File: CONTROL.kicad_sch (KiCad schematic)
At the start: 91 parts, among them J1 RJ45_Hanrun_HR911105A_Horizon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, J9 DISP, M1 Fan_4pin, M2 Fan_4pin, Q1 BSS138, Q2 BSS138, SW1 SW_Omron_B3F-315x, U1 TMP102xxDRL, U12 W5500, U13 TMP102xxDRL, X1 TXM25M0004322JBDDO00T

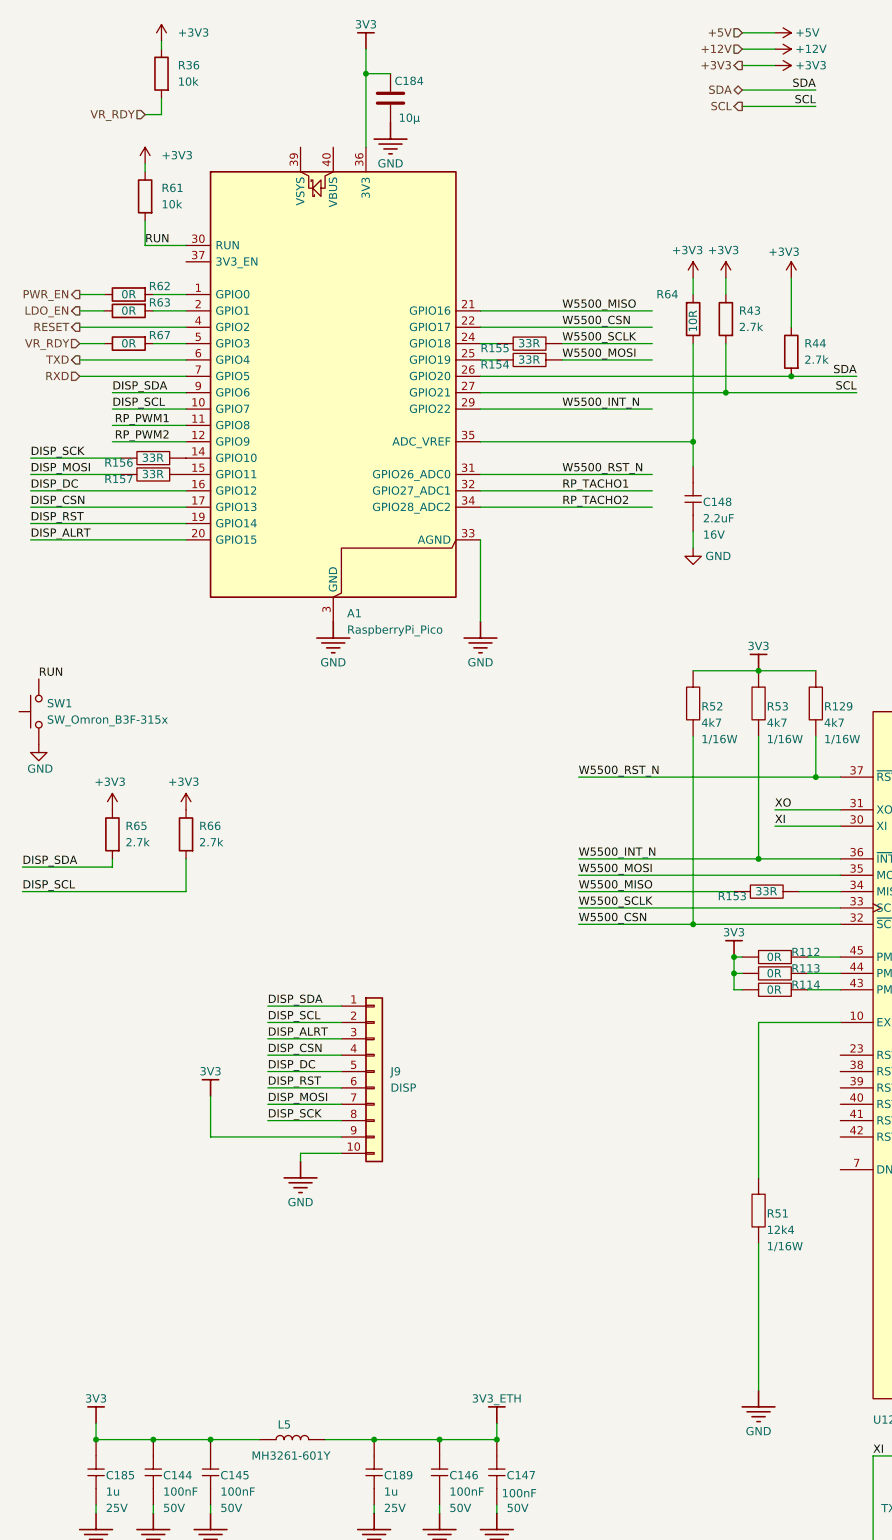
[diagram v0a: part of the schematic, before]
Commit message: W5500 ROUTED
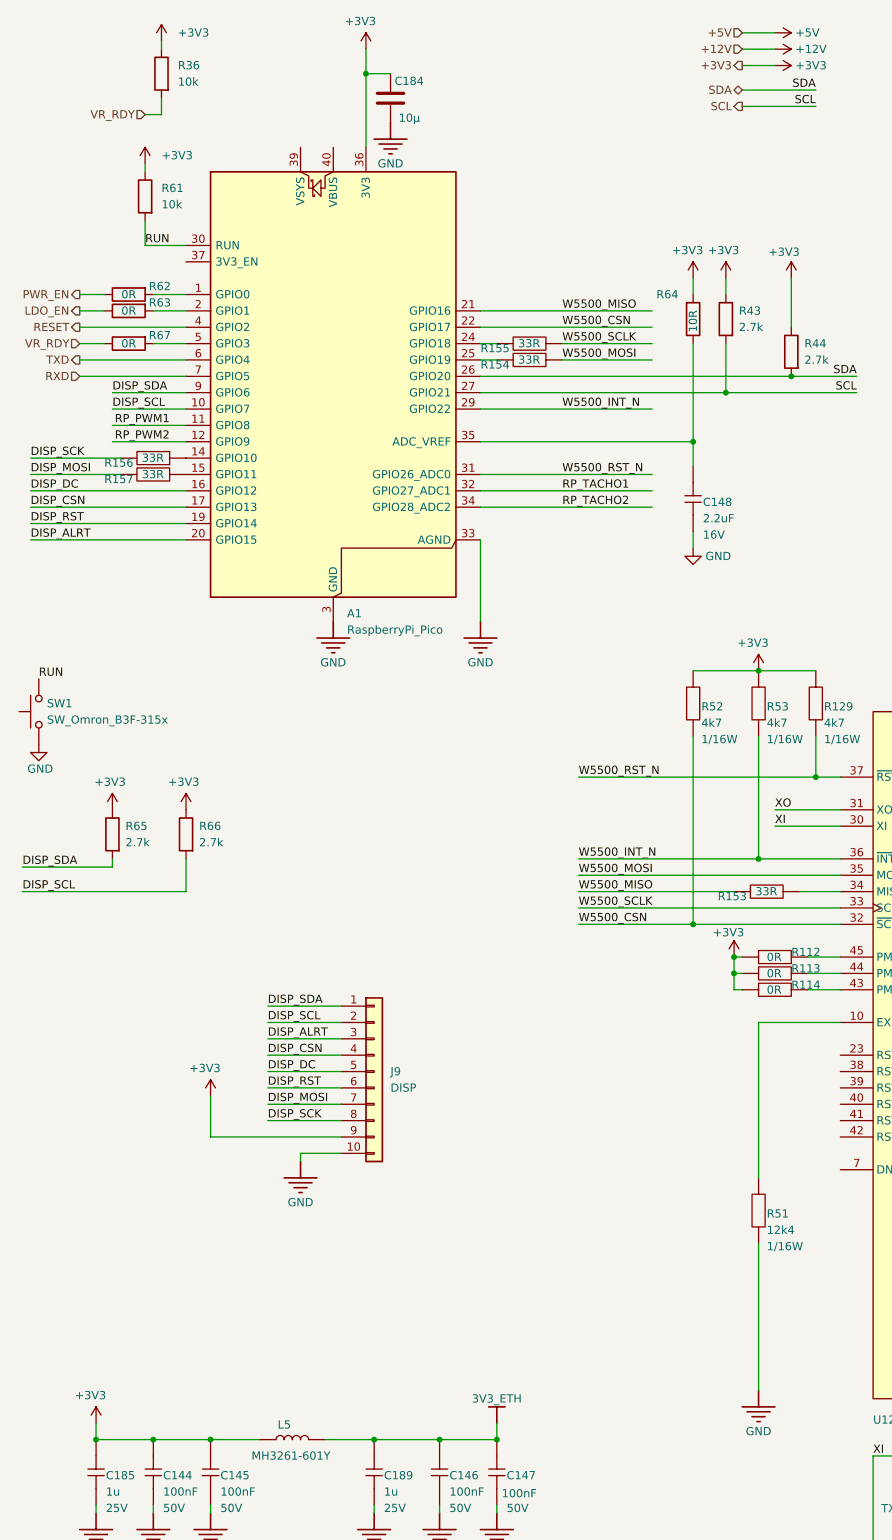
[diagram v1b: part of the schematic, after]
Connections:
- net 3V3 is gone; now on net +3V3: A1.36 (3V3), C144.1, C145.1, C184.1, C185.1, J9.9 (Pin_9), L5.1, R112.2, R113.2, R114.2, R129.2, R52.2, R53.2

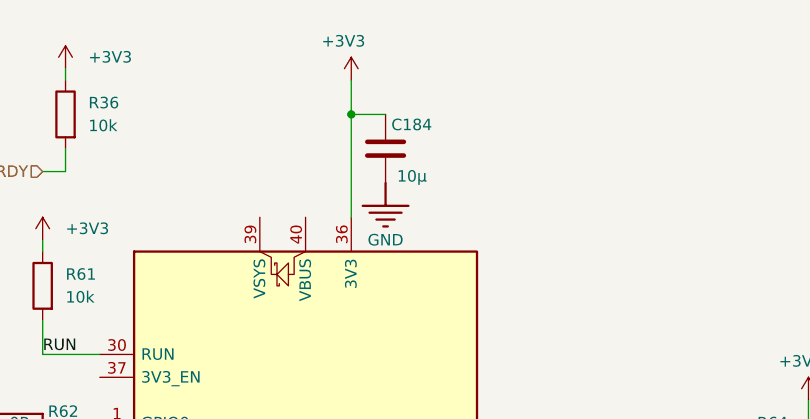
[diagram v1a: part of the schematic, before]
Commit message: logic dc bucks routed
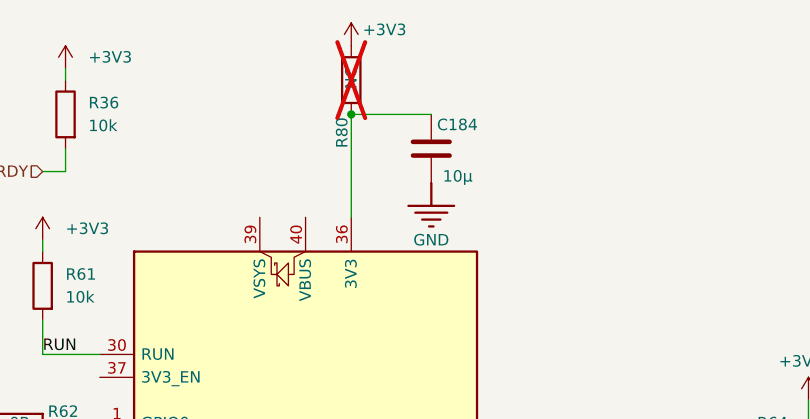
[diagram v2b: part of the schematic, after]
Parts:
- added R80: NC, Resistor_SMD:R_0603_1608Metric, symbol Device:R
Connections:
- net +3V3: now also R80.2; no longer A1.36 (3V3), C184.1
- new net: A1.36 (3V3), C184.1, R80.1
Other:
- moved on the sheet: C184
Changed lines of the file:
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@@
 	)
 	(junction
-		(at 72.39 25.4)
-		(diameter 0)
-		(color 0 0 0 0)
-	)
-	(junction
 		(at 234.95 167.64)
 		(diameter 0)
@@
 	)
 	(junction
+		(at 72.39 25.4)
+		(diameter 0)
+		(color 0 0 0 0)
+	)
+	(junction
 		(at 30.48 237.49)
 		(diameter 0)
@@
 	(wire
 		(pts
-			(xy 72.39 25.4) (xy 76.2 25.4)
+			(xy 72.39 25.4) (xy 81.28 25.4)
 		)
 		(stroke
@@
 	(wire
 		(pts
-			(xy 72.39 21.59) (xy 72.39 25.4)
-		)
-		(stroke
-			(width 0)
-			(type default)
-		)
-	)
-	(wire
-		(pts
 			(xy 83.82 248.92) (xy 83.82 247.65)
 		)
@@
 	(symbol
 		(lib_id "IMPORT-altium-import:GND_POWER_GROUND")
-		(at 76.2 33.02 0)
+		(at 81.28 33.02 0)
 		(unit 1)
 		(body_style 1)
@@
 		(dnp no)
 		(property "Reference" "#PWR0264"
-			(at 76.2 33.02 0)
+			(at 81.28 33.02 0)
 			(hide yes)
 			(show_name no)
@@
 		)
 		(property "Value" "GND"
-			(at 76.2 39.37 0)
+			(at 81.28 39.37 0)
 			(show_name no)
 			(do_not_autoplace no)
@@
 		)
 		(property "Footprint" ""
-			(at 76.2 33.02 0)
+			(at 81.28 33.02 0)
 			(show_name no)
 			(do_not_autoplace no)
@@
 		)
 		(property "Datasheet" ""
-			(at 76.2 33.02 0)
+			(at 81.28 33.02 0)
 			(show_name no)
 			(do_not_autoplace no)
@@
 		)
 		(property "Description" ""
-			(at 76.2 33.02 0)
+			(at 81.28 33.02 0)
 			(show_name no)
 			(do_not_autoplace no)
@@
 	)
 	(symbol
+		(lib_id "Device:R")
+		(at 72.39 21.59 0)
+		(mirror x)
+		(unit 1)
+		(body_style 1)
+		(exclude_from_sim no)
+		(in_bom yes)
+		(on_board yes)
+		(in_pos_files yes)
+		(dnp yes)
+		(property "Reference" "R80"
+			(at 71.374 27.432 90)
+			(show_name no)
+			(do_not_autoplace no)
+			(effects
+				(font
+					(size 1.27 1.27)
+				)
+			)
+		)
+		(property "Value" "NC"
+			(at 72.39 21.336 90)
+			(show_name no)
+			(do_not_autoplace no)
+			(effects
+				(font
+					(size 1.27 1.27)
+				)
+			)
+		)
+		(property "Footprint" "Resistor_SMD:R_0603_1608Metric"
+			(at 70.612 21.59 90)
+			(hide yes)
+			(show_name no)
+			(do_not_autoplace no)
+			(effects
+				(font
+					(size 1.27 1.27)
+				)
+			)
+		)
+		(property "Datasheet" ""
+			(at 72.39 21.59 0)
+			(hide yes)
+			(show_name no)
+			(do_not_autoplace no)
+			(effects
+				(font
+					(size 1.27 1.27)
+				)
+			)
+		)
+		(property "Description" "RES 10K OHM 1% 1/8W 0805"
+			(at 72.39 21.59 0)
+			(hide yes)
+			(show_name no)
+			(do_not_autoplace no)
+			(effects
+				(font
+					(size 1.27 1.27)
+				)
+			)
+		)
+		(property "Distributor" "D"
+			(at 72.39 21.59 0)
+			(hide yes)
+			(show_name no)
+			(do_not_autoplace no)
+			(effects
+				(font
+					(size 1.27 1.27)
+				)
+			)
+		)
+		(property "Manufacturer" "RMCF0805FT10K0"
+			(at 72.39 21.59 0)
+			(hide yes)
+			(show_name no)
+			(do_not_autoplace no)
+			(effects
+				(font
+					(size 1.27 1.27)
+				)
+			)
+		)
+		(property "OrderNr" "RMCF0805FT10K0CT-ND"
+			(at 72.39 21.59 0)
+			(hide yes)
+			(show_name no)
+			(do_not_autoplace no)
+			(effects
+				(font
+					(size 1.27 1.27)
+				)
+			)
+		)
+		(pin "1"
+		)
+		(pin "2"
+		)
+		(instances
+			(project "BRAIINS_AXE"
+				(path "/e63e39d7-6ac0-4ffd-8aa3-1841a4541b55/9bc1a7d6-07fa-4858-9423-fb2dbf7da294"
+					(reference "R80")
+					(unit 1)
+				)
+			)
+		)
+	)
+	(symbol
 		(lib_id "IMPORT-altium-import:GND_POWER_GROUND")
 		(at 342.9 229.87 0)
@@
 	(symbol
 		(lib_id "Device:C")
-		(at 76.2 29.21 0)
+		(at 81.28 29.21 0)
 		(unit 1)
 		(body_style 1)
@@
 		(dnp no)
 		(property "Reference" "C184"
-			(at 76.835 27.305 0)
+			(at 81.915 27.305 0)
 			(show_name no)
 			(do_not_autoplace no)
@@
 		)
 		(property "Value" "10µ"
-			(at 77.47 33.02 0)
+			(at 82.55 33.02 0)
 			(show_name no)
 			(do_not_autoplace no)
@@
 		)
 		(property "Footprint" "Capacitor_SMD:C_0805_2012Metric"
-			(at 76.2 29.21 0)
+			(at 81.28 29.21 0)
 			(hide yes)
 			(show_name no)
@@
 		)
 		(property "Datasheet" ""
-			(at 76.2 29.21 0)
+			(at 81.28 29.21 0)
 			(hide yes)
 			(show_name no)
@@
 		)
 		(property "Description" "CAP CER 10UF 25V X5R 0805"
-			(at 76.2 29.21 0)
+			(at 81.28 29.21 0)
 			(hide yes)
 			(show_name no)
@@
 		)
 		(property "DK" ""
-			(at 76.2 29.21 0)
+			(at 81.28 29.21 0)
 			(hide yes)
 			(show_name no)
@@
 		)
 		(property "PARTNO" ""
-			(at 76.2 29.21 0)
+			(at 81.28 29.21 0)
 			(hide yes)
 			(show_name no)
@@
 		)
 		(property "Distributor" "D"
-			(at 76.2 29.21 0)
+			(at 81.28 29.21 0)
 			(hide yes)
 			(show_name no)
@@
 		)
 		(property "Manufacturer" "C2012X5R1E106K125AB"
-			(at 76.2 29.21 0)
+			(at 81.28 29.21 0)
 			(hide yes)
 			(show_name no)
@@
 		)
 		(property "OrderNr" "445-5984-1-ND"
-			(at 76.2 29.21 0)
+			(at 81.28 29.21 0)
 			(hide yes)
 			(show_name no)
@@
 		(lib_name "+3V3_1")
 		(lib_id "power:+3V3")
-		(at 72.39 21.59 0)
+		(at 72.39 17.78 0)
 		(unit 1)
 		(body_style 1)
@@
 		(dnp no)
 		(property "Reference" "#PWR04007"
-			(at 72.39 25.4 0)
+			(at 72.39 21.59 0)
 			(hide yes)
 			(show_name no)
@@
 		)
 		(property "Value" "+3V3"
-			(at 69.088 17.272 0)
+			(at 73.66 16.002 0)
 			(show_name no)
 			(do_not_autoplace no)
@@
 		)
 		(property "Footprint" ""
-			(at 72.39 21.59 0)
+			(at 72.39 17.78 0)
 			(hide yes)
 			(show_name no)
@@
 		)
 		(property "Datasheet" ""
-			(at 72.39 21.59 0)
+			(at 72.39 17.78 0)
 			(hide yes)
 			(show_name no)
@@
 		)
 		(property "Description" "Power symbol creates a global label with name \"+3V3\""
-			(at 72.39 21.59 0)
+			(at 72.39 17.78 0)
 			(hide yes)
 			(show_name no)

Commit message: Change micro symbol to uF
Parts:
- C184: value 10µ -> 10uF
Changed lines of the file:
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@@
 			)
 		)
-		(property "Value" "10µ"
+		(property "Value" "10uF"
 			(at 82.55 33.02 0)
 			(show_name no)

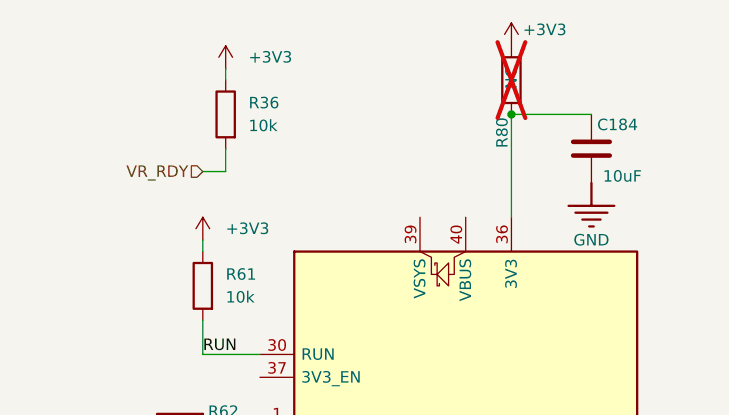
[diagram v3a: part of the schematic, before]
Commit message: Add schottky diode to rp pico vbus
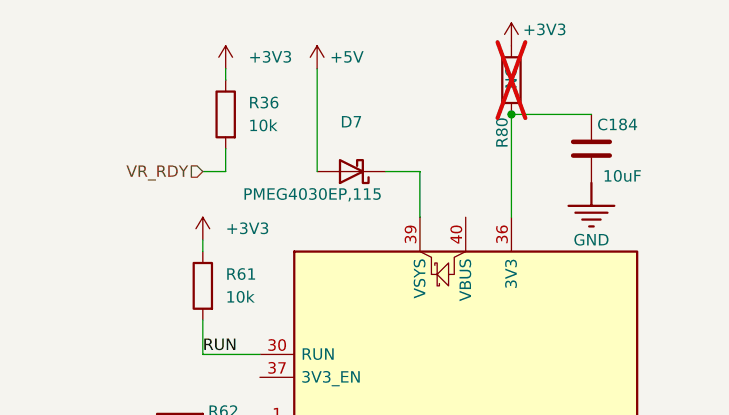
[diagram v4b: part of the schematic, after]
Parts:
- added D7: PMEG4030EP,115, Diode_SMD:D_SOD-128, symbol Device:D_Schottky
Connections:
- net +5V: now also D7.2 (A)
- net at A1.39 (VSYS): now also D7.1 (K)
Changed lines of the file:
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@@
 	(wire
 		(pts
+			(xy 50.8 20.32) (xy 50.8 31.75)
+		)
+		(stroke
+			(width 0)
+			(type default)
+		)
+	)
+	(wire
+		(pts
 			(xy 367.03 35.56) (xy 367.03 41.91)
 		)
@@
 	(wire
 		(pts
+			(xy 58.42 31.75) (xy 62.23 31.75)
+		)
+		(stroke
+			(width 0)
+			(type default)
+		)
+	)
+	(wire
+		(pts
 			(xy 307.34 24.13) (xy 318.77 24.13)
 		)
@@
 	(wire
 		(pts
+			(xy 62.23 31.75) (xy 62.23 36.83)
+		)
+		(stroke
+			(width 0)
+			(type default)
+		)
+	)
+	(wire
+		(pts
 			(xy 38.1 39.37) (xy 38.1 40.64)
 		)
@@
 	)
 	(symbol
+		(lib_id "power:+5V")
+		(at 50.8 20.32 0)
+		(unit 1)
+		(body_style 1)
+		(exclude_from_sim no)
+		(in_bom yes)
+		(on_board yes)
+		(in_pos_files yes)
+		(dnp no)
+		(property "Reference" "#PWR0183"
+			(at 50.8 24.13 0)
+			(hide yes)
+			(show_name no)
+			(do_not_autoplace no)
+			(effects
+				(font
+					(size 1.27 1.27)
+				)
+			)
+		)
+		(property "Value" "+5V"
+			(at 54.102 19.05 0)
+			(show_name no)
+			(do_not_autoplace no)
+			(effects
+				(font
+					(size 1.27 1.27)
+				)
+			)
+		)
+		(property "Footprint" ""
+			(at 50.8 20.32 0)
+			(hide yes)
+			(show_name no)
+			(do_not_autoplace no)
+			(effects
+				(font
+					(size 1.27 1.27)
+				)
+			)
+		)
+		(property "Datasheet" ""
+			(at 50.8 20.32 0)
+			(hide yes)
+			(show_name no)
+			(do_not_autoplace no)
+			(effects
+				(font
+					(size 1.27 1.27)
+				)
+			)
+		)
+		(property "Description" ""
+			(at 50.8 20.32 0)
+			(hide yes)
+			(show_name no)
+			(do_not_autoplace no)
+			(effects
+				(font
+					(size 1.27 1.27)
+				)
+			)
+		)
+		(pin "1"
+		)
+		(instances
+			(project "BRAIINS_AXE"
+				(path "/e63e39d7-6ac0-4ffd-8aa3-1841a4541b55/9bc1a7d6-07fa-4858-9423-fb2dbf7da294"
+					(reference "#PWR0183")
+					(unit 1)
+				)
+			)
+		)
+	)
+	(symbol
 		(lib_id "Switch:SW_Omron_B3FS")
 		(at 21.59 124.46 90)
@@
 	)
 	(symbol
+		(lib_id "Device:D_Schottky")
+		(at 54.61 31.75 180)
+		(unit 1)
+		(body_style 1)
+		(exclude_from_sim no)
+		(in_bom yes)
+		(on_board yes)
+		(in_pos_files yes)
+		(dnp no)
+		(property "Reference" "D7"
+			(at 54.61 26.2636 0)
+			(show_name no)
+			(do_not_autoplace no)
+			(effects
+				(font
+					(size 1.27 1.27)
+				)
+			)
+		)
+		(property "Value" "PMEG4030EP,115"
+			(at 50.292 34.29 0)
+			(show_name no)
+			(do_not_autoplace no)
+			(effects
+				(font
+					(size 1.27 1.27)
+				)
+			)
+		)
+		(property "Footprint" "Diode_SMD:D_SOD-128"
+			(at 54.61 31.75 0)
+			(hide yes)
+			(show_name no)
+			(do_not_autoplace no)
+			(effects
+				(font
+					(size 1.27 1.27)
+				)
+			)
+		)
+		(property "Datasheet" ""
+			(at 54.61 31.75 0)
+			(hide yes)
+			(show_name no)
+			(do_not_autoplace no)
+			(effects
+				(font
+					(size 1.27 1.27)
+				)
+			)
+		)
+		(property "Description" "DIODE SCHOTTKY 40V 3A SOD128"
+			(at 54.61 31.75 0)
+			(hide yes)
+			(show_name no)
+			(do_not_autoplace no)
+			(effects
+				(font
+					(size 1.27 1.27)
+				)
+			)
+		)
+		(property "Distributor" "D"
+			(at 54.61 31.75 0)
+			(hide yes)
+			(show_name no)
+			(do_not_autoplace no)
+			(effects
+				(font
+					(size 1.27 1.27)
+				)
+			)
+		)
+		(property "Manufacturer" "PMEG4030EP,115"
+			(at 54.61 31.75 0)
+			(hide yes)
+			(show_name no)
+			(do_not_autoplace no)
+			(effects
+				(font
+					(size 1.27 1.27)
+				)
+			)
+		)
+		(property "OrderNr" "1727-5841-1-ND"
+			(at 54.61 31.75 0)
+			(hide yes)
+			(show_name no)
+			(do_not_autoplace no)
+			(effects
+				(font
+					(size 1.27 1.27)
+				)
+			)
+		)
+		(pin "1"
+		)
+		(pin "2"
+		)
+		(instances
+			(project "BRAIINS_AXE"
+				(path "/e63e39d7-6ac0-4ffd-8aa3-1841a4541b55/9bc1a7d6-07fa-4858-9423-fb2dbf7da294"
+					(reference "D7")
+					(unit 1)
+				)
+			)
+		)
+	)
+	(symbol
 		(lib_id "IMPORT-altium-import:GND_POWER_GROUND")
 		(at 184.15 229.87 0)
@@
 		)
 	)
-	(embedded_fonts no)
 )

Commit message: Add LCSC number to components
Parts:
- A1: LCSC (none) -> C41407547
- C128, C129: LCSC (none) -> C519483
- C130, C131, C132, C134, C135, C136, C137, C138, C139, C144, C145, C146, C147: LCSC (none) -> C1591
- C133: LCSC (none) -> C69335
- C140, C141: LCSC (none) -> C1631
- C142: LCSC (none) -> C21122
- C143: LCSC (none) -> C106012
- C148: LCSC (none) -> C106853
- C149, C150: LCSC (none) -> C726567
- C184: LCSC (none) -> C318691
- C185, C189: LCSC (none) -> C29936
- C87, C88: LCSC (none) -> C694249
- D3, D4, D5: LCSC (none) -> C165701
- D7: LCSC (none) -> C96234
- J1: LCSC (none) -> C12074
- J9: LCSC (none) -> C492409
- L5: LCSC (none) -> C840591; MANUFACTURER Bourns Inc. -> (none); Manufacturer (none) -> Bourns Inc.
- M1, M2: LCSC (none) -> C240840
- Q1, Q2: LCSC (none) -> C52895
- R112, R113, R114, R62, R63, R67, R73, R76, R77, R79: LCSC (none) -> C2906974
- R129, R52, R53: LCSC (none) -> C218056
- R153, R154, R155, R156, R157: LCSC (none) -> C2909394
- R33, R35, R43, R44, R65, R66: LCSC (none) -> C2907008
- R36, R61, R74, R75: LCSC (none) -> C126901
- R41, R60: LCSC (none) -> C105578
- R42, R45, R46, R49: LCSC (none) -> C2930016
- R50, R54, R55, R56: LCSC (none) -> C2930110
- R51: LCSC (none) -> C2930060
- R57, R64: LCSC (none) -> C193335
- R58, R59: LCSC (none) -> C125768
- R68, R71: LCSC (none) -> C2784878
- SW1: LCSC (none) -> C231320
- U1, U13: LCSC (none) -> C2864144

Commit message: Use only stock component and unified LCSC capacitor code
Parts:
- C140, C141: LCSC C1631 -> C5137585
- C87, C88: LCSC C694249 -> C314282
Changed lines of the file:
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@@
 			)
 		)
-		(property "LCSC" "C694249"
+		(property "LCSC" "C314282"
 			(at 384.81 76.2 0)
 			(hide yes)
@@
 			)
 		)
-		(property "LCSC" "C1631"
+		(property "LCSC" "C5137585"
 			(at 261.62 167.64 0)
 			(hide yes)
@@
 			)
 		)
-		(property "LCSC" "C694249"
+		(property "LCSC" "C314282"
 			(at 384.81 40.64 0)
 			(hide yes)
@@
 			)
 		)
-		(property "LCSC" "C1631"
+		(property "LCSC" "C5137585"
 			(at 255.27 170.18 0)
 			(hide yes)
